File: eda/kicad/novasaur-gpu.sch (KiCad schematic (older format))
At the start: 21 parts, among them U1 74F86, U28 74F163, U29 74F163, U3 74F08, U30 74F541, U31 74F574, U32 74F574, U33 74F541, U34 74F574, U35 74F299, U36 74F574, U37 74F157

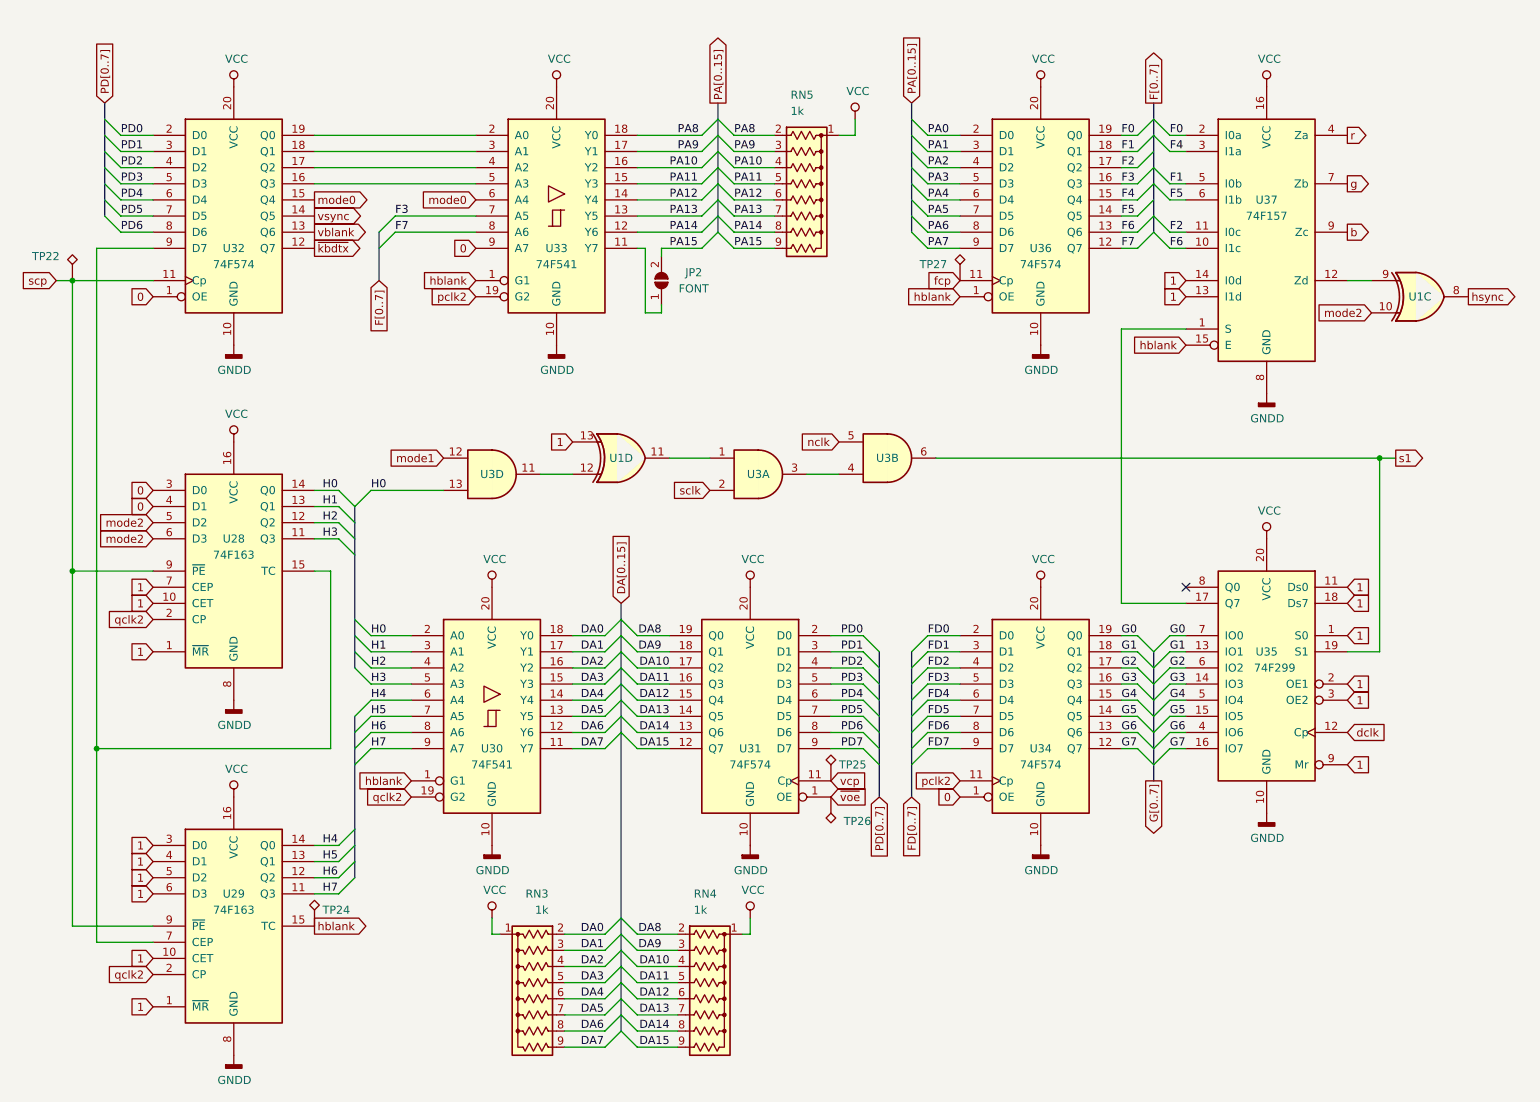
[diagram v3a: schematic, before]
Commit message: fix video timing debug and finish video modes
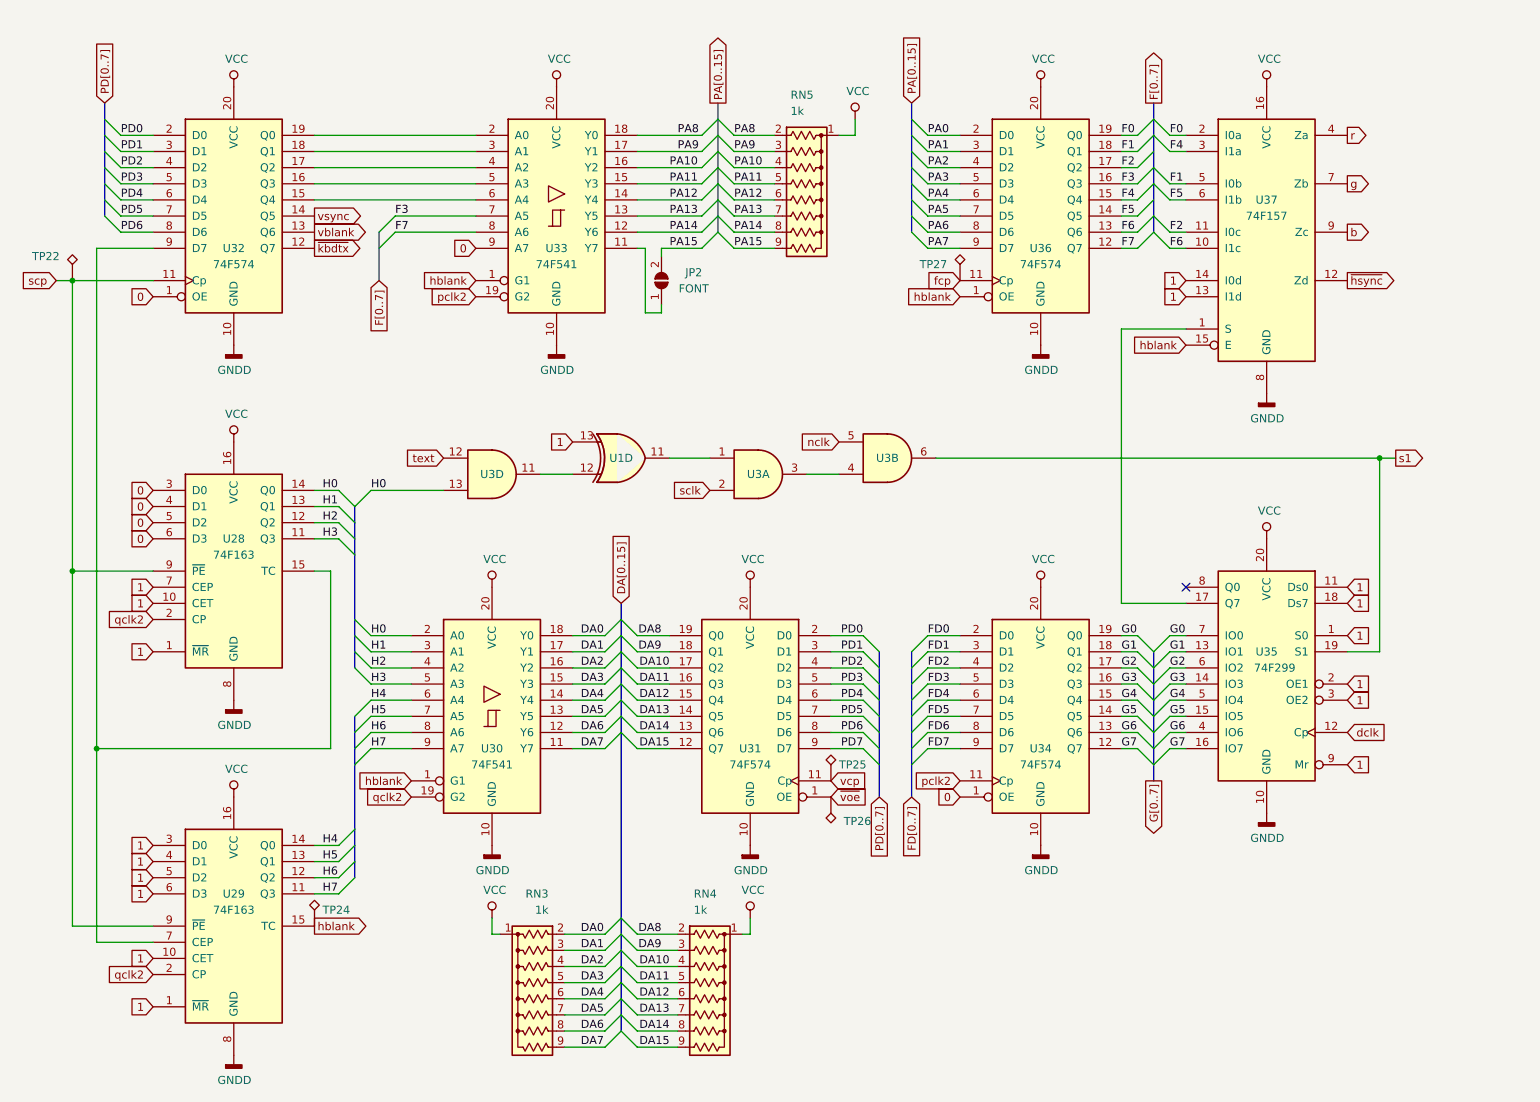
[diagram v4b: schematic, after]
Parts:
- removed unit 3 of U1
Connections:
- net mode2 is gone; now on net 0: U28.5 (D2), U28.6 (D3)
- net ~hsync: now reaches U37.12 (Zd)
- net mode0: no longer names the net of U32.15 (Q4), U33.6 (A4)
- net mode1 renamed text
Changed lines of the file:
@@
 Sheet 3 4
 Title "Graphics Processing Unit"
-Date "2020-08-20"
+Date "2020-09-10"
 Rev "1.7"
 Comp ""
@@
 $EndComp
 Text GLabel 3500 3550 0    50   Input ~ 0
-mode1
+text
 Text GLabel 1700 3850 0    50   Input ~ 0
 0
-Text GLabel 1700 3950 0    50   Input ~ 0
-mode2
 Text GLabel 1700 3750 0    50   Input ~ 0
 0
-Text GLabel 1700 4050 0    50   Input ~ 0
-mode2
 Wire Wire Line
 	2700 4250 2800 4250
@@
 	1    0    0    -1
 $EndComp
-Text GLabel 9250 2650 0    50   Input ~ 0
-mode2
 Text GLabel 1700 4750 0    50   Input ~ 0
 1
@@
 Wire Wire Line
 	7700 4450 8100 4450
-$Comp
-L 74xx:74LS86 U?
-U 3 1 5E79B6AD
-P 9550 2550
-AR Path="/5E79B6AD" Ref="U?"  Part="3"
-AR Path="/5DA1E9BD/5E79B6AD" Ref="U1"  Part="3"
-F 0 "U1" H 9550 2550 50  0000 C CNN
-F 1 "74F86" H 9550 2784 50  0001 C CNN
-F 2 "Package_DIP:DIP-14_W7.62mm_LongPads" H 9550 2550 50  0001 C CNN
-F 3 "74xx/74ls86.pdf" H 9550 2550 50  0001 C CNN
-	3    9550 2550
-	1    0    0    -1
-$EndComp
-Text GLabel 9850 2550 2    50   Output ~ 0
-hsync
+Text GLabel 9100 2450 2    50   Output ~ 0
+~hsync
 Wire Wire Line
 	5750 3650 5950 3650
@@
 Wire Wire Line
 	4700 2150 5100 2150
-Text GLabel 2700 1950 2    50   Output ~ 0
-mode0
-Text GLabel 3700 1950 0    50   Input ~ 0
-mode0
-Wire Wire Line
-	9100 2450 9250 2450
 Wire Wire Line
 	1350 2250 1700 2250
@@
 $EndComp
 Connection ~ 1200 2450
+Text GLabel 1700 4050 0    50   Input ~ 0
+0
+Text GLabel 1700 3950 0    50   Input ~ 0
+0
+Wire Wire Line
+	2700 1950 3700 1950
 Wire Bus Line
 	3100 2150 3100 2450

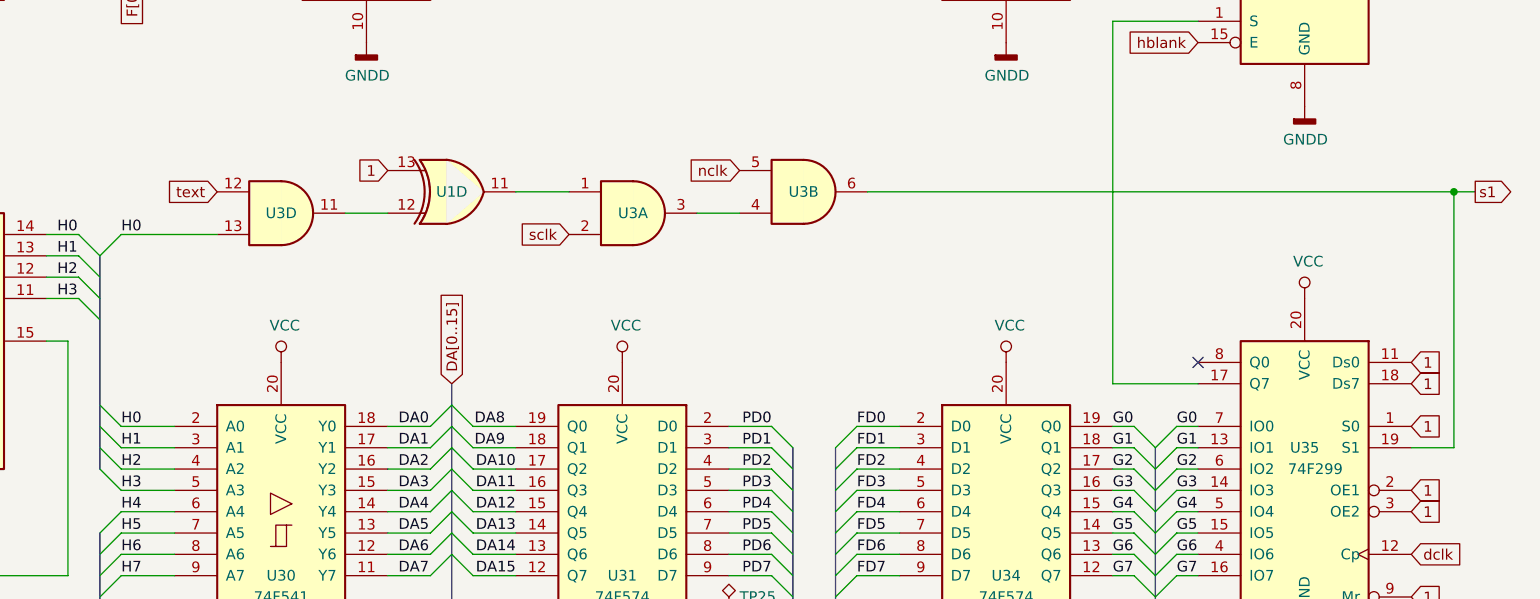
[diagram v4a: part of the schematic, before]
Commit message: Fix audio Updates to make audio work after testing
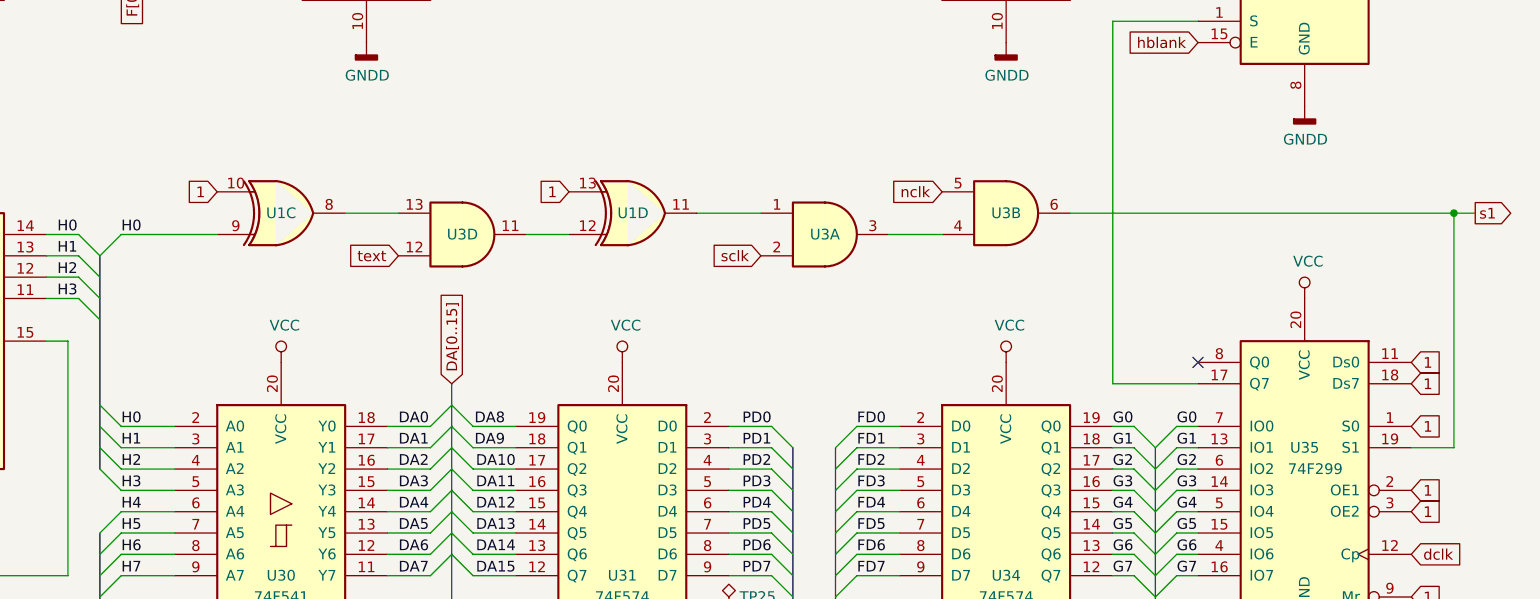
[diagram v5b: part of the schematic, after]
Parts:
- added unit 3 of U1
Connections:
- net 1: now also U1.10
- net H0: now also U1.9; no longer U3.13
- new net: U1.8, U3.13
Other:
- moved on the sheet: U1D, U3A, U3B, U3D
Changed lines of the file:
@@
 	1    0    0    -1
 $EndComp
-Text GLabel 3500 3550 0    50   Input ~ 0
+Text GLabel 4350 3850 0    50   Input ~ 0
 text
 Text GLabel 1700 3850 0    50   Input ~ 0
@@
 Wire Wire Line
 	5350 6500 5400 6500
-Text GLabel 2700 6450 2    50   Output ~ 0
-hblank
 Text GLabel 6200 5650 3    50   Input ~ 0
 PD[0..7]
@@
 Entry Wire Line
 	6100 5350 6200 5450
-Text GLabel 5950 3450 0    50   Input ~ 0
+Text GLabel 6900 3550 0    50   Input ~ 0
 nclk
-Text GLabel 5150 3750 0    50   Input ~ 0
+Text GLabel 6050 3850 0    50   Input ~ 0
 sclk
 Text Label 3050 3750 0    50   ~ 0
@@
 	1    7200 5150
 	1    0    0    -1
-$EndComp
-$Comp
-L Device:R_Network08_US RN4
-U 1 1 5D1C1196
-P 4050 6900
-AR Path="/5DAA3954/5D1C1196" Ref="RN4"  Part="1"
-AR Path="/5DAA5CD8/5D9A6C5F/5D1C1196" Ref="RN?"  Part="1"
-AR Path="/5DA1E9BD/5D1C1196" Ref="RN3"  Part="1"
-F 0 "RN3" V 3400 6800 50  0000 L CNN
-F 1 "1k" V 3500 6800 50  0000 L CNN
-F 2 "Resistor_THT:R_Array_SIP9" V 4525 6900 50  0001 C CNN
-F 3 "http://www.vishay.com/docs/31509/csc.pdf" H 4050 6900 50  0001 C CNN
-	1    4050 6900
-	0    -1   1    0
 $EndComp
 Text GLabel 1700 4550 0    50   Input ~ 0
@@
 Text GLabel 6700 5550 0    50   Input ~ 0
 pclk2
-Text GLabel 9400 3550 2    50   Output ~ 0
+Text GLabel 9400 3650 2    50   Output ~ 0
 s1
 Text GLabel 5900 5650 2    50   Input ~ 0
@@
 L 74xx:74LS08 U?
 U 2 1 5DCE5E0A
-P 6250 3550
+P 7200 3650
 AR Path="/5CDEEC9F/5DCE5E0A" Ref="U?"  Part="2"
 AR Path="/5DAA5CD8/5DCE5E0A" Ref="U?"  Part="2"
 AR Path="/5DCE5E0A" Ref="U?"  Part="2"
 AR Path="/5DA1E9BD/5DCE5E0A" Ref="U3"  Part="2"
-F 0 "U3" H 6250 3550 50  0000 C CNN
-F 1 "74F08" H 6250 3750 50  0001 C CNN
-F 2 "Package_DIP:DIP-14_W7.62mm_LongPads" H 6250 3550 50  0001 C CNN
-F 3 "http://www.ti.com/lit/gpn/sn74LS08" H 6250 3550 50  0001 C CNN
-	2    6250 3550
+F 0 "U3" H 7200 3650 50  0000 C CNN
+F 1 "74F08" H 7200 3850 50  0001 C CNN
+F 2 "Package_DIP:DIP-14_W7.62mm_LongPads" H 7200 3650 50  0001 C CNN
+F 3 "http://www.ti.com/lit/gpn/sn74LS08" H 7200 3650 50  0001 C CNN
+	2    7200 3650
 	1    0    0    1
 $EndComp
@@
 L 74xx:74LS08 U?
 U 1 1 5DCE5E10
-P 5450 3650
+P 6350 3750
 AR Path="/5CDEEC9F/5DCE5E10" Ref="U?"  Part="1"
 AR Path="/5DAA5CD8/5DCE5E10" Ref="U?"  Part="1"
 AR Path="/5DCE5E10" Ref="U?"  Part="1"
 AR Path="/5DA1E9BD/5DCE5E10" Ref="U3"  Part="1"
-F 0 "U3" H 5450 3650 50  0000 C CNN
-F 1 "74F08" H 5450 3450 50  0001 C CNN
-F 2 "Package_DIP:DIP-14_W7.62mm_LongPads" H 5450 3650 50  0001 C CNN
-F 3 "http://www.ti.com/lit/gpn/sn74LS08" H 5450 3650 50  0001 C CNN
-	1    5450 3650
+F 0 "U3" H 6350 3750 50  0000 C CNN
+F 1 "74F08" H 6350 3550 50  0001 C CNN
+F 2 "Package_DIP:DIP-14_W7.62mm_LongPads" H 6350 3750 50  0001 C CNN
+F 3 "http://www.ti.com/lit/gpn/sn74LS08" H 6350 3750 50  0001 C CNN
+	1    6350 3750
 	1    0    0    -1
 $EndComp
@@
 Text GLabel 1700 4750 0    50   Input ~ 0
 1
-Connection ~ 9300 3550
-Wire Wire Line
-	9300 3550 9400 3550
+Wire Wire Line
+	9300 3650 9400 3650
 $Comp
 L 74xx:74LS157 U?
@@
 Text GLabel 9100 2450 2    50   Output ~ 0
 ~hsync
-Wire Wire Line
-	5750 3650 5950 3650
-Wire Wire Line
-	9300 3550 9300 4750
-Text GLabel 4300 3450 0    50   Input ~ 0
+Text GLabel 5150 3550 0    50   Input ~ 0
 1
 $Comp
 L 74xx:74LS86 U?
 U 4 1 5E72FE45
-P 4600 3550
+P 5450 3650
 AR Path="/5E72FE45" Ref="U?"  Part="4"
 AR Path="/5DA1E9BD/5E72FE45" Ref="U1"  Part="4"
 AR Path="/5DA1E9BA/5E72FE45" Ref="U?"  Part="4"
-F 0 "U1" H 4600 3550 50  0000 C CNN
-F 1 "74F86" H 4600 3784 50  0001 C CNN
-F 2 "Package_DIP:DIP-14_W7.62mm_LongPads" H 4600 3550 50  0001 C CNN
-F 3 "74xx/74ls86.pdf" H 4600 3550 50  0001 C CNN
-	4    4600 3550
+F 0 "U1" H 5450 3650 50  0000 C CNN
+F 1 "74F86" H 5450 3884 50  0001 C CNN
+F 2 "Package_DIP:DIP-14_W7.62mm_LongPads" H 5450 3650 50  0001 C CNN
+F 3 "74xx/74ls86.pdf" H 5450 3650 50  0001 C CNN
+	4    5450 3650
 	1    0    0    1
 $EndComp
@@
 L 74xx:74LS08 U?
 U 4 1 5E79B5B5
-P 3800 3650
+P 4650 3750
 AR Path="/5DAA3954/5E79B5B5" Ref="U?"  Part="4"
 AR Path="/5DAA5CD8/5E79B5B5" Ref="U?"  Part="4"
@@
 AR Path="/5DA1E9BD/5E79B5B5" Ref="U3"  Part="4"
 AR Path="/5DA1E9C0/5E79B5B5" Ref="U?"  Part="4"
-F 0 "U3" H 3800 3650 50  0000 C CNN
-F 1 "74F08" H 3800 3450 50  0001 C CNN
-F 2 "Package_DIP:DIP-14_W7.62mm_LongPads" H 3800 3650 50  0001 C CNN
-F 3 "http://www.ti.com/lit/gpn/sn74LS08" H 3800 3650 50  0001 C CNN
-	4    3800 3650
-	1    0    0    -1
-$EndComp
-Wire Wire Line
-	6550 3550 9300 3550
+F 0 "U3" H 4650 3750 50  0000 C CNN
+F 1 "74F08" H 4650 3550 50  0001 C CNN
+F 2 "Package_DIP:DIP-14_W7.62mm_LongPads" H 4650 3750 50  0001 C CNN
+F 3 "http://www.ti.com/lit/gpn/sn74LS08" H 4650 3750 50  0001 C CNN
+	4    4650 3750
+	1    0    0    1
+$EndComp
 Wire Wire Line
 	3050 3750 3500 3750
 Wire Wire Line
-	4100 3650 4300 3650
-Wire Wire Line
-	4900 3550 5150 3550
+	4950 3750 5150 3750
 Text GLabel 2700 2250 2    50   Output ~ 0
 ~kbdtx
@@
 Wire Wire Line
 	2700 1950 3700 1950
+Text GLabel 2700 6450 2    50   Output ~ 0
+hblank
+$Comp
+L Device:R_Network08_US RN4
+U 1 1 5D1C1196
+P 4050 6900
+AR Path="/5DAA3954/5D1C1196" Ref="RN4"  Part="1"
+AR Path="/5DAA5CD8/5D9A6C5F/5D1C1196" Ref="RN?"  Part="1"
+AR Path="/5DA1E9BD/5D1C1196" Ref="RN3"  Part="1"
+F 0 "RN3" V 3400 6800 50  0000 L CNN
+F 1 "1k" V 3500 6800 50  0000 L CNN
+F 2 "Resistor_THT:R_Array_SIP9" V 4525 6900 50  0001 C CNN
+F 3 "http://www.vishay.com/docs/31509/csc.pdf" H 4050 6900 50  0001 C CNN
+	1    4050 6900
+	0    -1   1    0
+$EndComp
+$Comp
+L 74xx:74LS86 U?
+U 3 1 5F723456
+P 3800 3650
+AR Path="/5F723456" Ref="U?"  Part="3"
+AR Path="/5DA1E9BD/5F723456" Ref="U1"  Part="3"
+F 0 "U1" H 3800 3650 50  0000 C CNN
+F 1 "74F86" H 3800 3884 50  0001 C CNN
+F 2 "Package_DIP:DIP-14_W7.62mm_LongPads" H 3800 3650 50  0001 C CNN
+F 3 "74xx/74ls86.pdf" H 3800 3650 50  0001 C CNN
+	3    3800 3650
+	1    0    0    1
+$EndComp
+Text GLabel 3500 3550 0    50   Input ~ 0
+1
+Wire Wire Line
+	9300 3650 9300 4750
+Connection ~ 9300 3650
+Wire Wire Line
+	4100 3650 4350 3650
+Wire Wire Line
+	6650 3750 6900 3750
+Wire Wire Line
+	7500 3650 9300 3650
+Wire Wire Line
+	5750 3650 6050 3650
 Wire Bus Line
 	3100 2150 3100 2450
